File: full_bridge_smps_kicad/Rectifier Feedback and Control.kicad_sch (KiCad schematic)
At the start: 32 parts, among them J6 Conn_01x04_Male, J7 Conn_01x02_Male, U1 MSP430F2012IPW, U1 TPS3809I50DBV, U3 OPA333AID

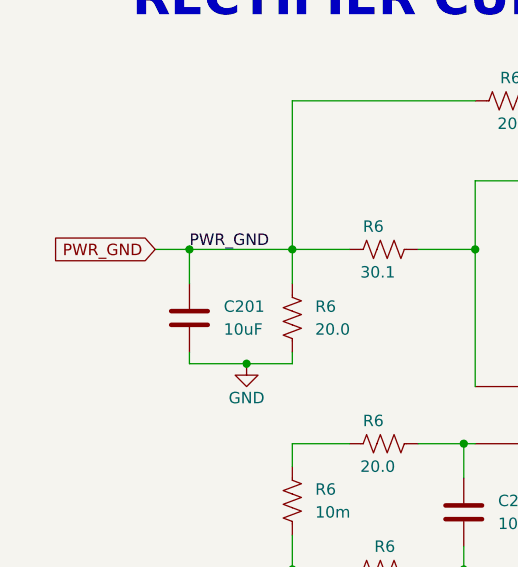
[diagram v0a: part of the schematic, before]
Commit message: Adding schematic page for interleaved CCM PFC
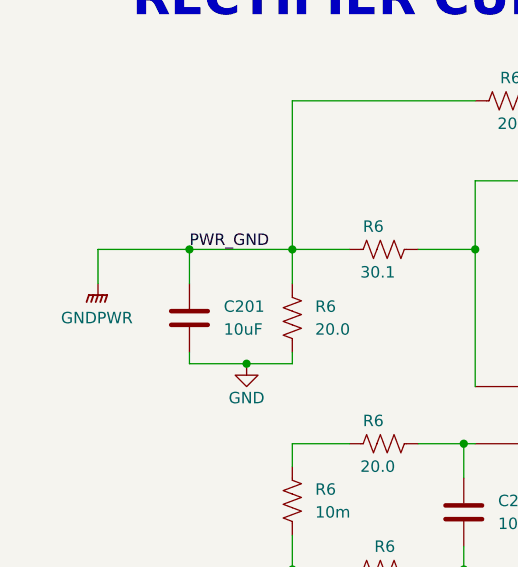
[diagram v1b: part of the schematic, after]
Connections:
- net PWR_GND renamed GNDPWR

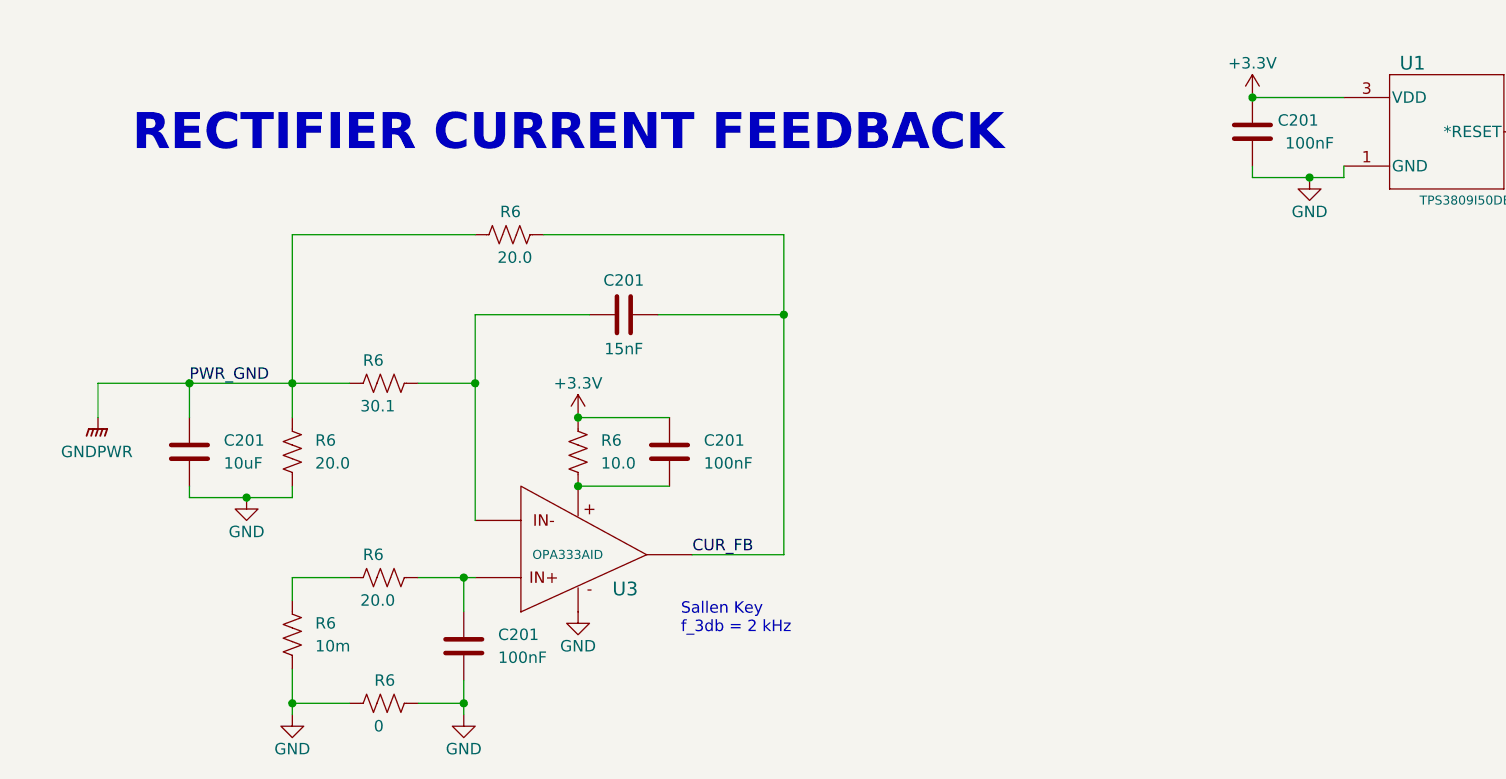
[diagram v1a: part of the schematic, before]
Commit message: Finishing up the output rectification, creating new pages for the corresponding feedback and drive circuits
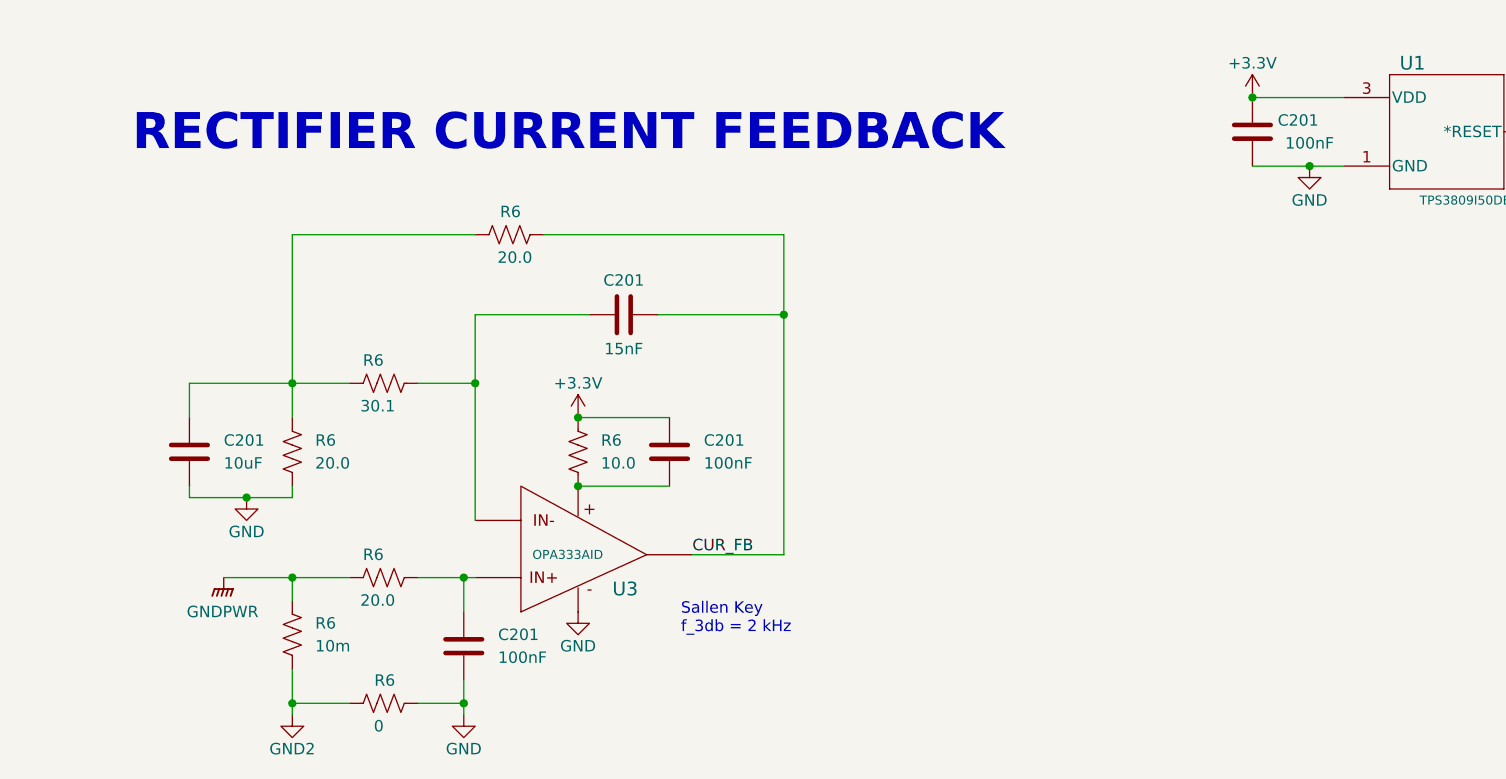
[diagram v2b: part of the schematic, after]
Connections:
- net GND: no longer R6.1, R6.2
- net GNDPWR: now also R6.1, R6.1; no longer C201.1, R6.1, R6.1, R6.1
- new net: C201.1, R6.1, R6.1, R6.1
- new net GND2: R6.1, R6.2
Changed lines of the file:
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@@
   (junction (at 81.28 158.75) (diameter 0) (color 0 0 0 0)
   )
+  (junction (at 162.56 123.19) (diameter 0) (color 0 0 0 0)
+  )
   (junction (at 68.58 168.91) (diameter 0) (color 0 0 0 0)
   )
@@
   (junction (at 140.97 52.07) (diameter 0) (color 0 0 0 0)
   )
-  (junction (at 38.1 147.32) (diameter 0) (color 0 0 0 0)
-  )
   (junction (at 156.21 115.57) (diameter 0) (color 0 0 0 0)
   )
   (junction (at 88.9 93.98) (diameter 0) (color 0 0 0 0)
   )
+  (junction (at 49.53 168.91) (diameter 0) (color 0 0 0 0)
+  )
   (junction (at 38.1 60.96) (diameter 0) (color 0 0 0 0)
   )
@@
   )
   (junction (at 104.14 139.7) (diameter 0) (color 0 0 0 0)
-  )
-  (junction (at 162.56 124.46) (diameter 0) (color 0 0 0 0)
   )
   (junction (at 44.45 93.98) (diameter 0) (color 0 0 0 0)
@@
     (stroke (width 0) (type default))
   )
-  (wire (pts (xy 27.94 147.32) (xy 38.1 147.32))
-    (stroke (width 0) (type default))
-  )
   (wire (pts (xy 49.53 130.81) (xy 69.85 130.81))
     (stroke (width 0) (type default))
   )
-  (wire (pts (xy 162.56 124.46) (xy 166.37 124.46))
+  (wire (pts (xy 162.56 123.19) (xy 166.37 123.19))
     (stroke (width 0) (type default))
   )
@@
     (stroke (width 0) (type default))
   )
-  (wire (pts (xy 156.21 123.19) (xy 156.21 124.46))
-    (stroke (width 0) (type default))
-  )
   (wire (pts (xy 38.1 60.96) (xy 44.45 60.96))
     (stroke (width 0) (type default))
@@
     (stroke (width 0) (type default))
   )
+  (wire (pts (xy 41.91 168.91) (xy 49.53 168.91))
+    (stroke (width 0) (type default))
+  )
   (wire (pts (xy 219.71 120.65) (xy 227.33 120.65))
     (stroke (width 0) (type default))
@@
     (stroke (width 0) (type default))
   )
-  (wire (pts (xy 27.94 147.32) (xy 27.94 151.13))
-    (stroke (width 0) (type default))
-  )
   (wire (pts (xy 49.53 147.32) (xy 55.88 147.32))
     (stroke (width 0) (type default))
@@
     (stroke (width 0) (type default))
   )
-  (wire (pts (xy 156.21 124.46) (xy 162.56 124.46))
+  (wire (pts (xy 156.21 123.19) (xy 162.56 123.19))
     (stroke (width 0) (type default))
   )
@@
   )
   (wire (pts (xy 247.65 73.66) (xy 260.35 73.66))
-    (stroke (width 0) (type default))
-  )
-  (wire (pts (xy 166.37 124.46) (xy 166.37 123.19))
     (stroke (width 0) (type default))
   )
@@
   )
   (label "CUR_FB" (at 143.51 59.69 0) (fields_autoplaced)
-    (effects (font (size 1.27 1.27)) (justify left bottom))
-  )
-  (label "PWR_GND" (at 38.1 147.32 0) (fields_autoplaced)
     (effects (font (size 1.27 1.27)) (justify left bottom))
   )
@@
     )
   )
-  (symbol (lib_id "power:GNDPWR") (at 27.94 151.13 0) (unit 1)
-    (in_bom yes) (on_board yes) (dnp no) (fields_autoplaced)
-    (property "Reference" "#PWR040" (at 27.94 156.21 0)
-      (effects (font (size 1.27 1.27)) hide)
-    )
-    (property "Value" "GNDPWR" (at 27.813 154.94 0)
-      (effects (font (size 1.27 1.27)))
-    )
-    (property "Footprint" "" (at 27.94 152.4 0)
-      (effects (font (size 1.27 1.27)) hide)
-    )
-    (property "Datasheet" "" (at 27.94 152.4 0)
-      (effects (font (size 1.27 1.27)) hide)
-    )
-    (pin "1")
-    (instances
-      (project "full_bridge_smps"
-        (path "/f89200e7-8fc9-4acb-bb2b-7da3a53d52f5/c7dd24b6-4b1e-4a6b-9e8e-5cce0d372c9a"
-          (reference "#PWR040") (unit 1)
-        )
-        (path "/f89200e7-8fc9-4acb-bb2b-7da3a53d52f5/e997b072-89af-4305-9e32-2a6ea6e450e3"
-          (reference "#PWR041") (unit 1)
-        )
-      )
-    )
-  )
   (symbol (lib_id "Device:R_US") (at 81.28 154.94 0) (unit 1)
     (in_bom yes) (on_board yes) (dnp no)
@@
     )
   )
+  (symbol (lib_id "power:GND2") (at 49.53 184.15 0) (unit 1)
+    (in_bom yes) (on_board yes) (dnp no)
+    (property "Reference" "#PWR09" (at 49.53 190.5 0)
+      (effects (font (size 1.27 1.27)) hide)
+    )
+    (property "Value" "GND2" (at 49.53 187.96 0)
+      (effects (font (size 1.27 1.27)))
+    )
+    (property "Footprint" "" (at 49.53 184.15 0)
+      (effects (font (size 1.27 1.27)) hide)
+    )
+    (property "Datasheet" "" (at 49.53 184.15 0)
+      (effects (font (size 1.27 1.27)) hide)
+    )
+    (pin "1")
+    (instances
+      (project "full_bridge_smps"
+        (path "/f89200e7-8fc9-4acb-bb2b-7da3a53d52f5/21f308e5-6ef4-4d74-8629-c11c93821636"
+          (reference "#PWR09") (unit 1)
+        )
+        (path "/f89200e7-8fc9-4acb-bb2b-7da3a53d52f5/e997b072-89af-4305-9e32-2a6ea6e450e3"
+          (reference "#PWR030") (unit 1)
+        )
+      )
+    )
+  )
   (symbol (lib_id "Device:R_US") (at 96.52 88.9 0) (unit 1)
     (in_bom yes) (on_board yes) (dnp no)
@@
     )
   )
-  (symbol (lib_id "power:GND") (at 49.53 184.15 0) (unit 1)
-    (in_bom yes) (on_board yes) (dnp no)
-    (property "Reference" "#PWR019" (at 49.53 190.5 0)
-      (effects (font (size 1.27 1.27)) hide)
-    )
-    (property "Value" "GND" (at 49.53 187.96 0)
-      (effects (font (size 1.27 1.27)))
-    )
-    (property "Footprint" "" (at 49.53 184.15 0)
-      (effects (font (size 1.27 1.27)) hide)
-    )
-    (property "Datasheet" "" (at 49.53 184.15 0)
-      (effects (font (size 1.27 1.27)) hide)
-    )
-    (pin "1")
-    (instances
-      (project "full_bridge_smps"
-        (path "/f89200e7-8fc9-4acb-bb2b-7da3a53d52f5/21f308e5-6ef4-4d74-8629-c11c93821636"
-          (reference "#PWR019") (unit 1)
-        )
-        (path "/f89200e7-8fc9-4acb-bb2b-7da3a53d52f5/e997b072-89af-4305-9e32-2a6ea6e450e3"
-          (reference "#PWR030") (unit 1)
-        )
-        (path "/f89200e7-8fc9-4acb-bb2b-7da3a53d52f5/c7dd24b6-4b1e-4a6b-9e8e-5cce0d372c9a"
-          (reference "#PWR042") (unit 1)
-        )
-      )
-    )
-  )
   (symbol (lib_id "fb_smps_symbols:TPS3809I50DBV") (at 166.37 113.03 0) (unit 1)
     (in_bom yes) (on_board yes) (dnp no)
@@
     )
   )
-  (symbol (lib_id "power:GND") (at 162.56 124.46 0) (unit 1)
-    (in_bom yes) (on_board yes) (dnp no)
-    (property "Reference" "#PWR037" (at 162.56 130.81 0)
-      (effects (font (size 1.27 1.27)) hide)
-    )
-    (property "Value" "GND" (at 162.56 128.27 0)
-      (effects (font (size 1.27 1.27)))
-    )
-    (property "Footprint" "" (at 162.56 124.46 0)
-      (effects (font (size 1.27 1.27)) hide)
-    )
-    (property "Datasheet" "" (at 162.56 124.46 0)
+  (symbol (lib_id "power:GND") (at 162.56 123.19 0) (unit 1)
+    (in_bom yes) (on_board yes) (dnp no)
+    (property "Reference" "#PWR037" (at 162.56 129.54 0)
+      (effects (font (size 1.27 1.27)) hide)
+    )
+    (property "Value" "GND" (at 162.56 127 0)
+      (effects (font (size 1.27 1.27)))
+    )
+    (property "Footprint" "" (at 162.56 123.19 0)
+      (effects (font (size 1.27 1.27)) hide)
+    )
+    (property "Datasheet" "" (at 162.56 123.19 0)
       (effects (font (size 1.27 1.27)) hide)
     )
@@
         )
       )
+    )
+  )
+  (symbol (lib_id "power:GNDPWR") (at 41.91 168.91 0) (unit 1)
+    (in_bom yes) (on_board yes) (dnp no) (fields_autoplaced)
+    (property "Reference" "#PWR040" (at 41.91 173.99 0)
+      (effects (font (size 1.27 1.27)) hide)
+    )
+    (property "Value" "GNDPWR" (at 41.783 172.72 0)
+      (effects (font (size 1.27 1.27)))
+    )
+    (property "Footprint" "" (at 41.91 170.18 0)
+      (effects (font (size 1.27 1.27)) hide)
+    )
+    (property "Datasheet" "" (at 41.91 170.18 0)
+      (effects (font (size 1.27 1.27)) hide)
+    )
+    (pin "1")
+    (instances
+      (project "full_bridge_smps"
+        (path "/f89200e7-8fc9-4acb-bb2b-7da3a53d52f5/c7dd24b6-4b1e-4a6b-9e8e-5cce0d372c9a"
+          (reference "#PWR040") (unit 1)
+        )
+        (path "/f89200e7-8fc9-4acb-bb2b-7da3a53d52f5/e997b072-89af-4305-9e32-2a6ea6e450e3"
+          (reference "#PWR080") (unit 1)
+        )
+      )

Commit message: A bit of refactoring, saving work for the day
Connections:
- net +3V3: no longer C201.1
- net GND: now also C201.2
- net V+: now also C201.1; no longer C201.2
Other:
- moved on the sheet: C201, C5, D2A, D2B, D3A, D3B, J6, J7, R1, R14, R15, R6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
